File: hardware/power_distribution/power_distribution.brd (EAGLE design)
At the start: 100.3 x 78.4 mm, 29 parts, among them Q1 MOSFET-NCHANNELFQP30N06L, Q2 MOSFET-NCHANNELFQP30N06L, U1 LTC4412ES6PBF, U10 ATMEGA328P_PDIP, U2 LTC4412ES6PBF, U3 ACS712, U4 ACS712, U5 MAX233, U6 MAX233, X1 53048-04, X4 53048-04, X5 53048-04, Y1 16MHz

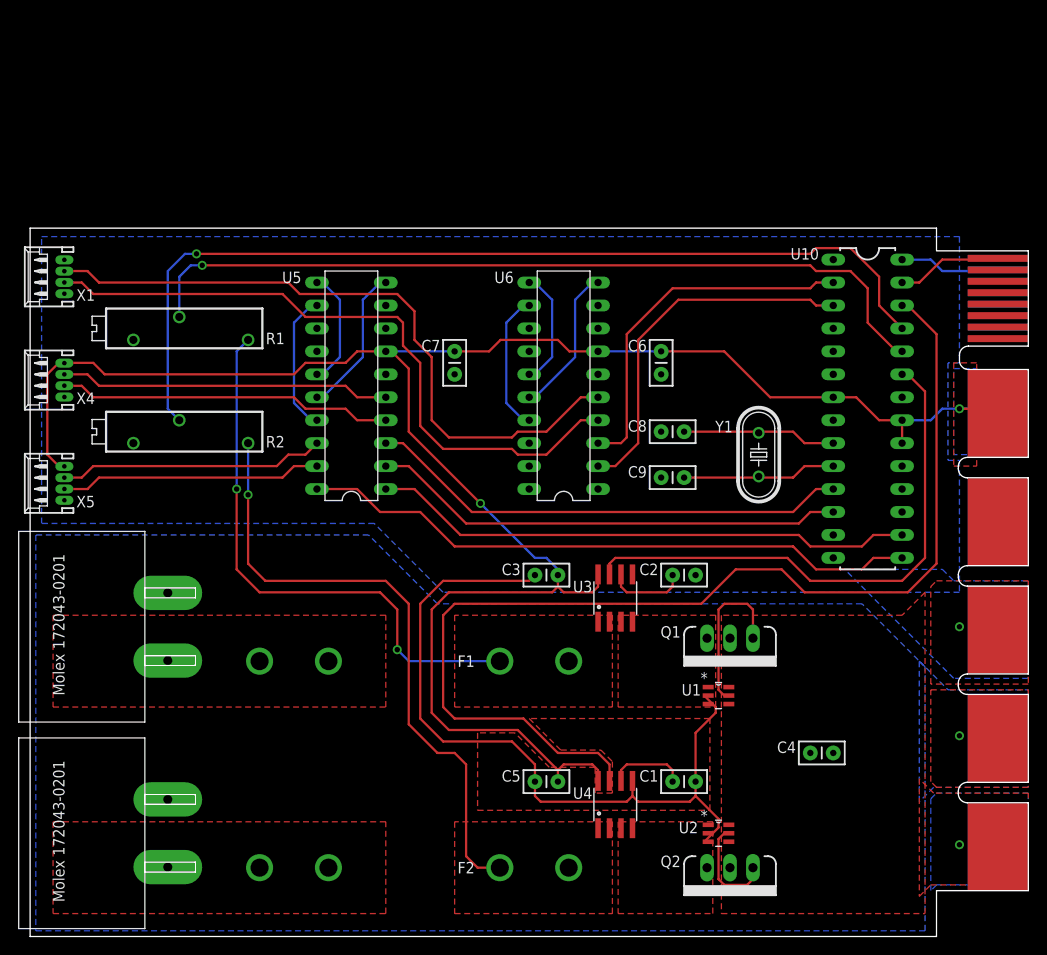
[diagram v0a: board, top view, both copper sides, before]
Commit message: Balances battery voltages and outputs one combined voltage
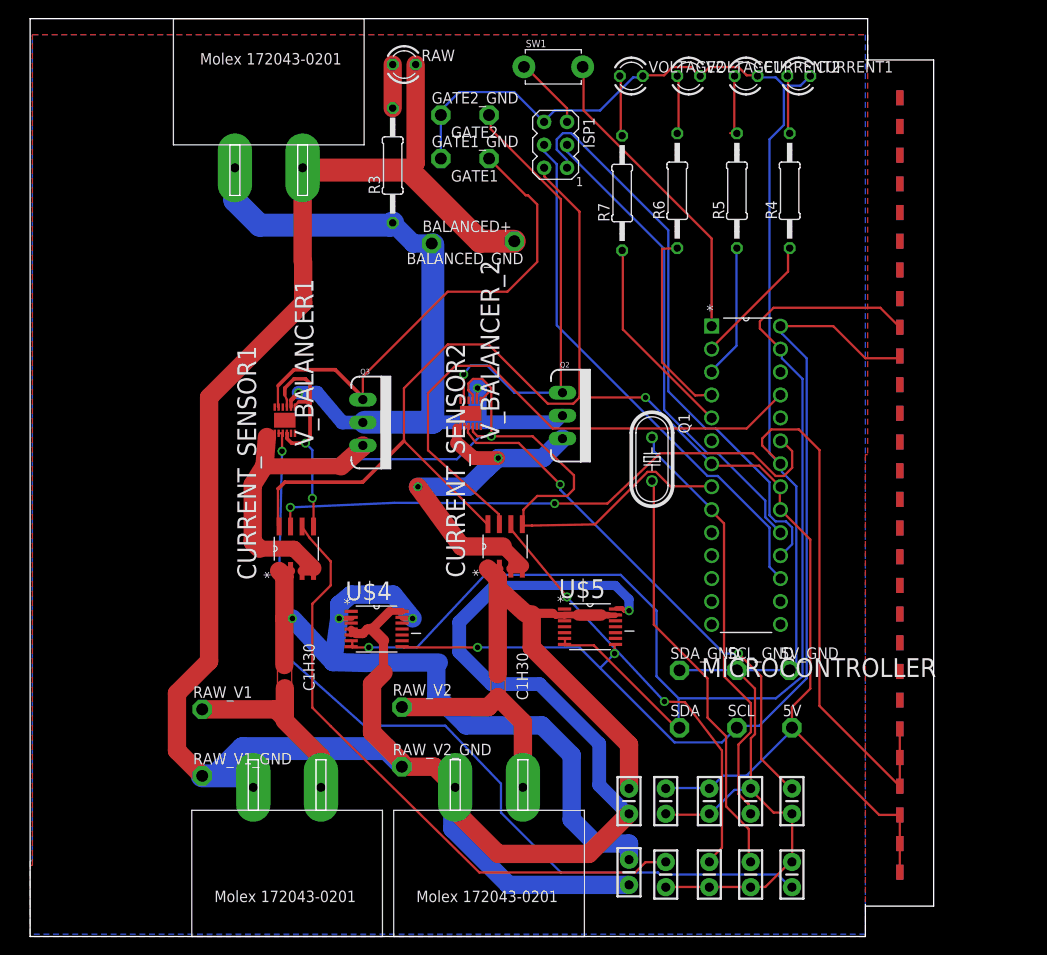
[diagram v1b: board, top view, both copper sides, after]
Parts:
- removed F1, F2: FUSE-HOLDER, fuse-holder:FUSE_HOLDER
- removed JP1: CARD_EDGE, Molex_Edge_2:EDGE_CONNECTOR
- removed R1, R2: 10k, resistor:RTRIM43P
- removed U1, U2: LTC4412ES6PBF, LTC_By_element14_Batch_1:SOT95P280X100-6N
- removed U10: ATMEGA328P_PDIP, SparkFun-DigitalIC:DIL28-3
- removed U3, U4: ACS712, SparkFun-AnalogIC:SO08
- removed U5, U6: MAX233, maxim:DIL20
- removed X1, X4, X5: 53048-04, con-molex:53048-04
- removed Y1: 16MHz, crystal:HC49U-V
- added 5V, 5V_GND, BALANCED+, BALANCED_GND, GATE1, GATE1_GND, GATE2, GATE2_GND, RAW_V1, RAW_V1_GND, RAW_V2, RAW_V2_GND, SCL, SCL_GND, SDA, SDA_GND: TPPAD1-13, testpad:P1-13
- added C10: 0.1uF, SparkFun-Capacitors:CAP-PTH-SMALL-KIT
- added CURRENT1, CURRENT2, RAW, VOLTAGE1, VOLTAGE2: (no value), led:LED3MM
- added CURRENT_SENSOR1, CURRENT_SENSOR2: ACS712ELCTR-05B-T, Allegro_By_element14_Batch_1:SOIC127P600X175-8N
- added INPUT1, INPUT2, OUTPUT: MOLEX172043-0201, Molex172043-0201:MOLEX172043-0201
- added ISP1: AVRISP-6, adafruit:AVRISP
- added MICROCONTROLLER: ATMEGA168P-20PU, Atmel_By_element14_Batch_1-00:DIP254P762X457-28
- added Q3: 60V/32A/35mΩ, SparkFun-DiscreteSemi:TO220V
- added R3, R4, R5, R6, R7: (no value), resistor:0207/12
- added SW1: (no value), adafruit:TACT_PANA-EVQ
- added U$3: 1-530844-7, 1-530844-7-PCBEDGE:1-530844-7
- added U$4, U$5: ADM1293, Analog Devices_By_element14_Batch_1:SOP65P640X120-14N
- added V_BALANCER1, V_BALANCER_2: LTC4352CDDPBF, LTC_By_element14_Batch_1:DFN300X300X80-13N
- C1, C2, C3: device SparkFun-Capacitors:CAP-PTH-SMALLEZ -> SparkFun-Capacitors:CAP-PTH-SMALL-KIT
- C4: value (none) -> 0.1uF; device SparkFun-Capacitors:CAP-PTH-SMALLEZ -> SparkFun-Capacitors:CAP-PTH-SMALL-KIT
- C5: value 0.1uF -> 20pF; device SparkFun-Capacitors:CAP-PTH-SMALLEZ -> SparkFun-Capacitors:CAP-PTH-SMALL-KIT
- C6: value 1.0uF -> 20pF; device SparkFun-Capacitors:CAP-PTH-SMALLEZ -> SparkFun-Capacitors:CAP-PTH-SMALL-KIT
- C7: value 1.0uF -> 0.1uF; device SparkFun-Capacitors:CAP-PTH-SMALLEZ -> SparkFun-Capacitors:CAP-PTH-SMALL-KIT
- C8, C9: value 20pF -> 0.1uF; device SparkFun-Capacitors:CAP-PTH-SMALLEZ -> SparkFun-Capacitors:CAP-PTH-SMALL-KIT
- Q1: value MOSFET-NCHANNELFQP30N06L -> (none); device SparkFun-DiscreteSemi:TO220V -> crystal:HC49U-V
- Q2: value MOSFET-NCHANNELFQP30N06L -> 60V/32A/35mΩ
- U$1, U$2: value MOLEX172043-0201 -> C1H30; device Molex172043-0201:MOLEX172043-0201 -> fuse:C1H30
- moved C7 62.2 mm to (84.3, 15.0)
- moved C6 58.8 mm to (79.8, 6.86)
- moved Q2 53.4 mm to (58.9, 57.7), turned to 270 degrees
- moved C8 51.1 mm to (84.3, 6.86), turned to 90 degrees
- moved C9 43.8 mm to (66.3, 7.11), turned to 270 degrees
- moved U$2 42.5 mm to (52.6, 26.2)
- moved C2 33.2 mm to (70.4, 6.86), turned to 270 degrees
- moved C3 30.1 mm to (75.2, 15.0), turned to 270 degrees
- moved Q1 21.6 mm to (68.8, 52.8), turned to 270 degrees
- moved C5 21.4 mm to (79.8, 15.0), turned to 90 degrees
- moved C4 19.2 mm to (75.2, 6.86), turned to 270 degrees
- moved U$1 17.7 mm to (29.0, 27.2)
- moved C1 2.29 mm to (70.4, 15.0), turned to 270 degrees
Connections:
- removed net B+: C4.1, JP1.1, JP1.14, Q1.2, Q2.2, U1.6, U2.6
- removed net B-: C4.2, JP1.15, JP1.2, U$1.PIN2, U$2.PIN2
- removed net B1+: F1.P$1, F1.P$2, U$1.PIN1
- removed net B1F+: F1.P$3, F1.P$4, R1.1, U3.1, U3.2
- removed net B1RX232: U5.4, X4.3
- removed net B1TX232: U5.5, X4.2
- removed net B2+: F2.P$1, F2.P$2, U$2.PIN1
- removed net B2F+: F2.P$3, F2.P$4, R2.1, U4.1, U4.2
- removed net B2RX232: U5.19, X5.3
- removed net B2TX232: U5.18, X5.2
- removed net C2+B: U5.11, U5.15
- removed net C2+CPU: U6.11, U6.15
- removed net C2-B: U5.10, U5.16
- removed net C2-CPU: U6.10, U6.16
- removed net CPU232RX: U6.4, X1.3
- removed net CPU232TX: U6.5, X1.2
- removed net FILT1: C2.1, U3.6
- removed net FILT2: C1.1, U4.6
- removed net RX1SOFT: U10.11, U5.3
- removed net RX2SOFT: U10.15, U5.20
- removed net RXD: U10.2, U6.3
- removed net TX1SOFT: U10.12, U5.2
- removed net TX2SOFT: U10.16, U5.1
- removed net TXD: U10.3, U6.2
- removed net V-B: U5.12, U5.17
- removed net V-CPU: U6.12, U6.17
- removed net VDIV1: R1.2, U10.24
- removed net VDIV2: R2.2, U10.25
- removed net VIN1: Q1.3, U1.1, U3.3, U3.4
- removed net VIN2: Q2.3, U2.1, U4.3, U4.4
- removed net VOUT1: U10.23, U3.7
- removed net VOUT2: U10.26, U4.7
- removed net XOSC1: C8.2, U10.9, Y1.1
- removed net XOSC2: C9.2, U10.10, Y1.2
- new net CURRENT_LED1: MICROCONTROLLER.2, R4.1
- new net CURRENT_LED2: MICROCONTROLLER.3, R5.1
- new net CURRENT_SIG1: CURRENT_SENSOR1.7, MICROCONTROLLER.23
- new net CURRENT_SIG2: CURRENT_SENSOR2.7, MICROCONTROLLER.25
- new net MISO: ISP1.1, MICROCONTROLLER.18
- new net MOSI: ISP1.4, MICROCONTROLLER.17
- new net N$1: C9.1, CURRENT_SENSOR1.1, CURRENT_SENSOR1.2, U$1.P$2, U$4.13, U$4.2
- new net N$10: INPUT1.PIN1, RAW_V1.TP, U$1.P$1
- new net N$11: C10.1, CURRENT_SENSOR2.1, CURRENT_SENSOR2.2, U$2.P$2, U$5.13, U$5.2
- new net N$13: CURRENT2.A, R5.2
- new net N$14: C2.1, CURRENT_SENSOR1.6
- new net N$15: R6.2, VOLTAGE1.A
- new net N$16: INPUT2.PIN1, RAW_V2.TP, U$2.P$1
- new net N$17: R7.2, VOLTAGE2.A
- new net N$18: C4.1, CURRENT_SENSOR2.6
- new net N$19: BALANCED_GND.TP, C10.2, C9.2, INPUT1.PIN2, INPUT2.PIN2, OUTPUT.PIN2, RAW.K, RAW_V1_GND.TP, RAW_V2_GND.TP, U$4.14, U$4.4, U$4.5, U$5.14
- new net N$2: C5.1, MICROCONTROLLER.9, Q1.1
- new net N$26: BALANCED+.TP, OUTPUT.PIN1, Q2.2, Q3.2, R3.1, V_BALANCER1.8, V_BALANCER_2.8
- new net N$27: MICROCONTROLLER.1, SW1.P$2
- new net N$3: C7.1, V_BALANCER_2.2, V_BALANCER_2.3
- new net N$4: C6.1, Q1.2
- new net N$5: CURRENT_SENSOR1.3, CURRENT_SENSOR1.4, Q3.3, V_BALANCER1.1
- new net N$7: CURRENT1.A, R4.2
- new net N$8: R3.2, RAW.A
- new net N$9: C8.1, V_BALANCER1.2, V_BALANCER1.3
- new net RESET_SW: ISP1.5, SW1.P$1
- new net SCK: ISP1.3, MICROCONTROLLER.19
- new net VOLTAGE_IN2: CURRENT_SENSOR2.3, CURRENT_SENSOR2.4, Q2.3, V_BALANCER_2.1
- new net VOLTAGE_LED1: MICROCONTROLLER.4, R6.1
- new net VOLTAGE_LED2: MICROCONTROLLER.5, R7.1
- net GATE1: now also GATE1.TP, Q3.1, V_BALANCER1.11; no longer Q1.1, U1.5
- net GATE2: now also GATE2.TP, V_BALANCER_2.11; no longer U2.5
- net GND: now also 5V_GND.TP, C4.2, C8.2, CURRENT1.K, CURRENT2.K, CURRENT_SENSOR1.5, CURRENT_SENSOR2.5, GATE1_GND.TP, GATE2_GND.TP, ISP1.6, MICROCONTROLLER.22, MICROCONTROLLER.8, SCL_GND.TP, SDA_GND.TP, U$3.P$32, U$3.P$33, U$3.P$34, U$3.P$4, U$3.P$5, U$3.P$6, VOLTAGE1.K, VOLTAGE2.K, V_BALANCER1.4, V_BALANCER1.7, V_BALANCER1.9, V_BALANCER_2.4, V_BALANCER_2.7, V_BALANCER_2.9; no longer C8.1, C9.1, JP1.16, JP1.3, R1.3, R2.3, U1.2, U1.3, U10.22, U10.8, U2.2, U2.3, U3.5, U4.5, U5.6, U5.9, U6.6, U6.9, X1.4, X4.4, X5.4
- net SCL: now also MICROCONTROLLER.28, SCL.TP, U$3.P$19, U$4.8, U$5.8; no longer JP1.12, JP1.25, U10.28
- net SDA: now also MICROCONTROLLER.27, SDA.TP, U$3.P$20, U$4.6, U$4.7, U$5.6, U$5.7; no longer JP1.13, JP1.26, U10.27
- net VCC: now also 5V.TP, C1.1, CURRENT_SENSOR1.8, CURRENT_SENSOR2.8, ISP1.2, MICROCONTROLLER.20, MICROCONTROLLER.21, MICROCONTROLLER.7, U$3.P$1, U$3.P$2, U$3.P$29, U$3.P$3, U$3.P$30, U$3.P$31; no longer C5.1, C6.1, C7.1, JP1.18, JP1.5, U10.20, U10.21, U10.7, U3.8, U4.8, U5.7, U6.7, X4.1, X5.1
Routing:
- net N$19: track 0.00 -> 287.0 mm, vias 0 -> 1
- net GND: track 86.3 -> 350.6 mm, vias 1 -> 3
- net SDA: track 11.7 -> 143.9 mm, vias 0 -> 1
- net VOUT2: track 122.7 -> 0.00 mm
- net VDIV2: track 104.9 -> 0.00 mm, vias 1 -> 0
- net SCL: track 11.2 -> 110.4 mm, vias 0 -> 2
- net N$9: track 0.00 -> 93.8 mm, vias 0 -> 1
- net VDIV1: track 91.2 -> 0.00 mm, vias 1 -> 0
- net N$1: track 0.00 -> 88.3 mm, vias 0 -> 3
- net N$26: track 0.00 -> 85.5 mm, vias 0 -> 2
- net CPU232TX: track 74.5 -> 0.00 mm
- net CPU232RX: track 74.1 -> 0.00 mm
- net N$14: track 0.00 -> 69.3 mm
- net RX2SOFT: track 69.0 -> 0.00 mm
- net B2F+: track 69.0 -> 0.00 mm, vias 1 -> 0
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- added copper zone on layer 1, net N$6
- removed copper zone on layer 1, net B+
- removed copper zone on layer 16, net B+
- removed copper zone on layer 1, net B-
- removed copper zone on layer 16, net B-
- removed copper zone on layer 1, net B1+
- removed copper zone on layer 1, net B1F+
- removed copper zone on layer 1, net B2+
- removed copper zone on layer 1, net B2F+
- removed copper zone on layer 1, net GND
- removed copper zone on layer 1, net VCC
- removed copper zone on layer 16, net VCC
- removed copper zone on layer 1, net VIN1
- removed copper zone on layer 1, net VIN2
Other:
- board size 100.3 x 78.4 mm -> 92.7 x 101.6 mm
- board text removed: "F1"
- board text removed: "F2"
